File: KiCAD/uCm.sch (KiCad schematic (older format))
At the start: 29 parts, among them P1 AREF, P4 ICSP, P5 FTDI, SW1 Reset, SW2 INT0, SW3 INT1, U7 ATMEGA328-AU-ND, X1 16MHz

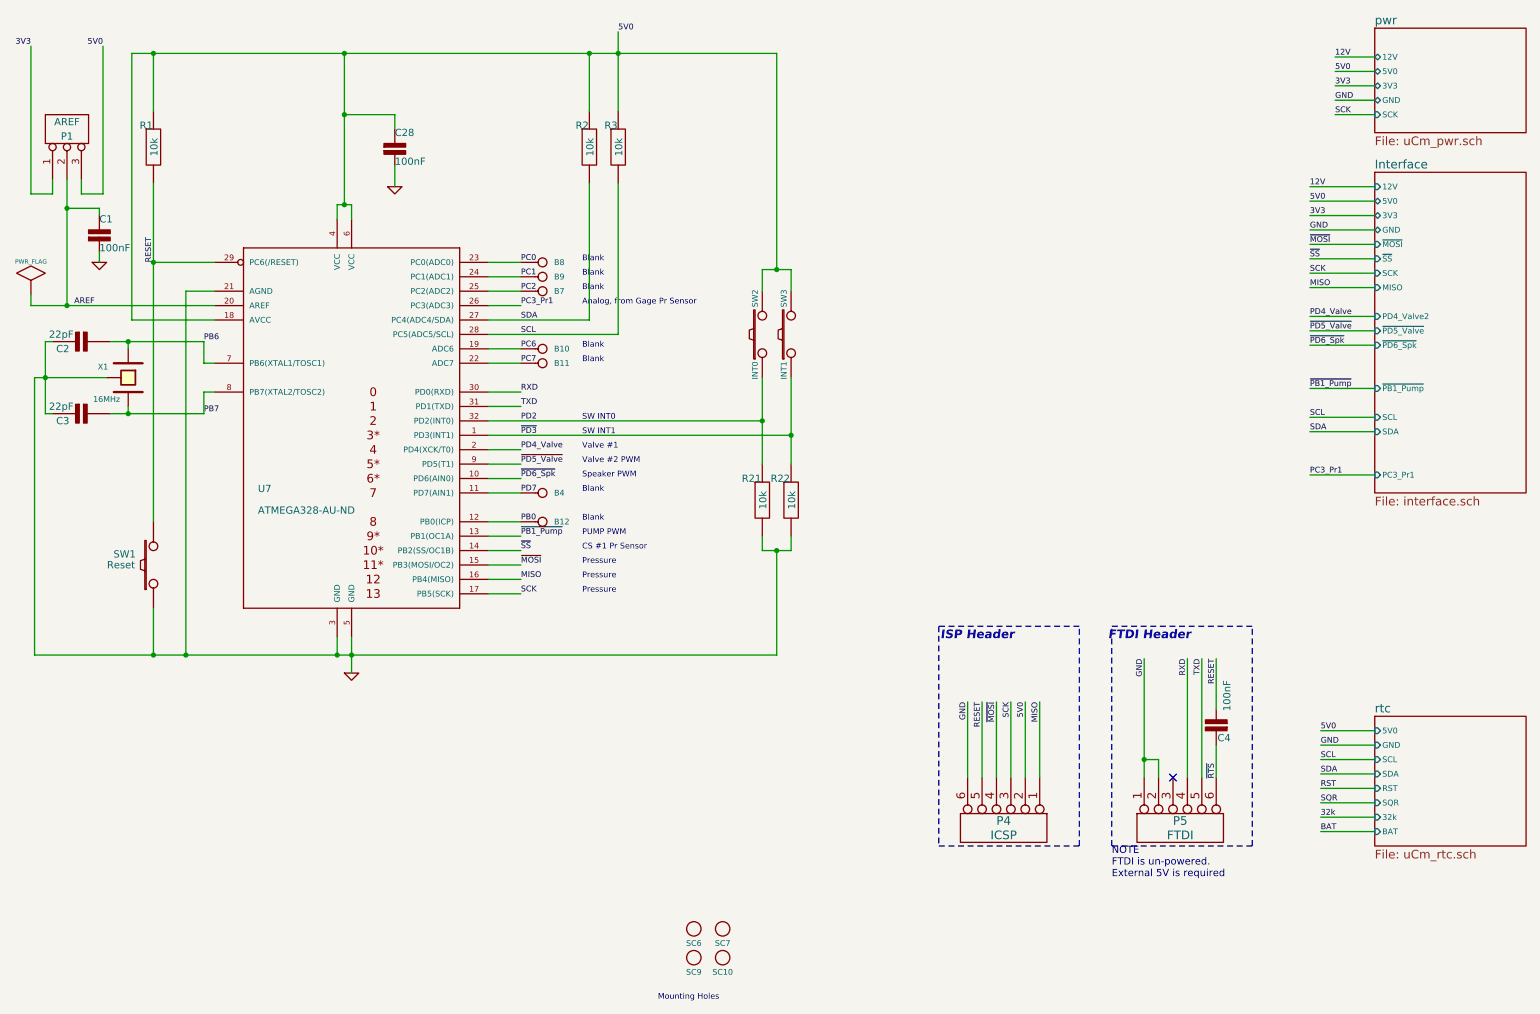
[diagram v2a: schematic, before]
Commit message: changed power supply section
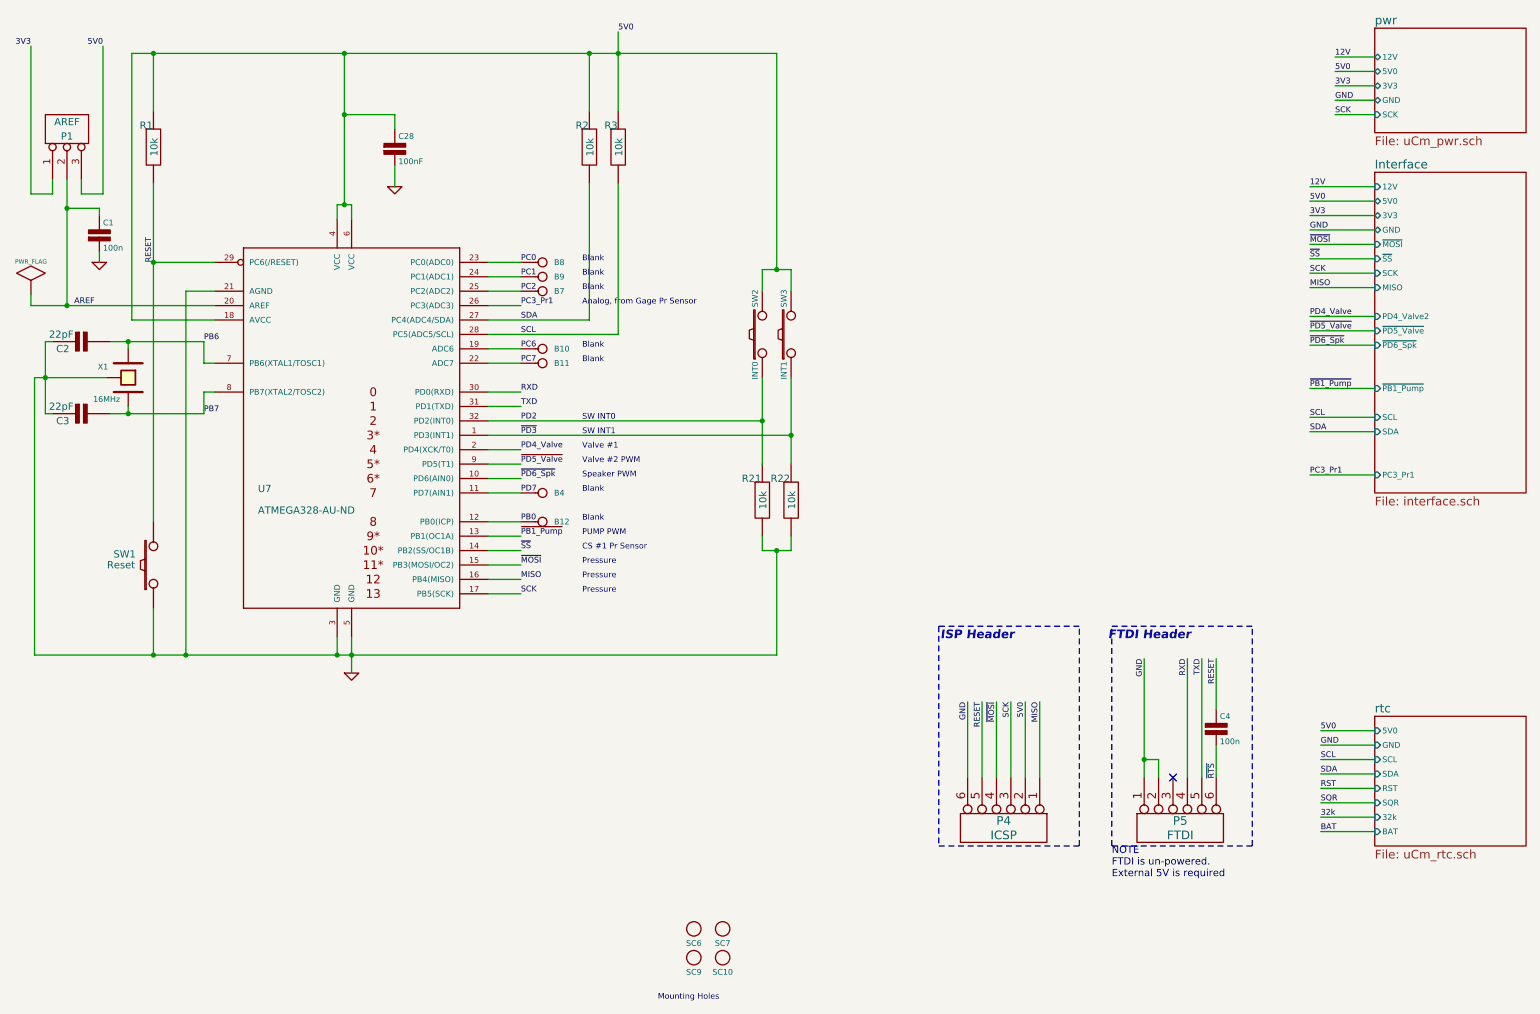
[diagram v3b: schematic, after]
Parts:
- C1, C4: value 100nF -> 100n; footprint uCm:c_0805 -> (none); Field10 399-5863-ND -> (none); Field11 http://www.digikey.com/product-detail/en/R82DC3100AA50J/399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 -> (none); Field4 CAP FILM 0.1UF 63VDC RADIAL -> (none); Field5 100nF, 63V -> (none); Field6 R82 -> (none); Field7 Kemet -> (none); Field8 R82DC3100AA50J -> (none); Field9 Digikey -> (none); manf# (none) -> CL21B104KCC5PNC
- C2, C3: Field10 BC1034CT-ND -> (none); Field11 http://www.digikey.com/product-detail/en/K220J15C0GF5TH5/BC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 -> (none); Field4 CAP CER 22PF 50V 5% RADIAL -> (none); Field5 22pF, 50V -> (none); Field6 Radial -> (none); Field7 Vishay BC Components -> (none); Field8 K220J15C0GF5TH5 -> (none); Field9 Digikey -> (none); manf# (none) -> CL10C220JB8NNNC
- C28: Field10 399-5863-ND -> (none); Field11 http://www.digikey.com/product-detail/en/R82DC3100AA50J/399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 -> (none); Field4 CAP FILM 0.1UF 63VDC RADIAL -> (none); Field5 100nF, 63V -> (none); Field6 R82 -> (none); Field7 Kemet -> (none); Field8 R82DC3100AA50J -> (none); Field9 Digikey -> (none); manf# (none) -> CL21B104KCC5PNC
- P1: Field10 SAM1031-50-ND -> (none); Field11 http://www.digikey.com/scripts/DkSearch/dksus.dll?WT.z_head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 -> (none); Field4 CONN HEADER 50POS .100\" SGL GOLD -> (none); Field5 Header, Unshrouded, Male pin, -> (none); Field6 0.1\" pitch x 50 nos -> (none); Field7 Samtec Inc -> (none); Field8 TSW-150-07-L-S -> (none); Field9 Digikey -> (none)
- P4: Field10 609-3210-ND -> (none); Field11 http://www.digikey.com/scripts/DkSearch/dksus.dll?vendor=0&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 -> (none); Field4 CONN HEADER 6POS .100 STR 15AU -> (none); Field5 Header, Unshrouded, Male Pin -> (none); Field6 6 pos, 2 row, 0.1\" -> (none); Field7 FCI -> (none); Field8 67996-206HLF -> (none); Field9 Digikey -> (none); manf# (none) -> PREC003DAAN-RC
- P5: manf# (none) -> PREC006SAAN-RC
- R1, R2, R21, R22, R3: Field10 CF18JT10K0CT-ND -> (none); Field11 http://www.digikey.com/product-detail/en/CF18JT10K0/CF18JT1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 -> (none); Field4 RES 10K OHM 1/8W 5% CF AXIAL -> (none); Field5 0.125W, 1/8W -> (none); Field6 Axial -> (none); Field7 Stackpole Electronics Inc -> (none); Field8 CF18JT10K0 -> (none); Field9 Digikey -> (none); manf# (none) -> RMCF0805JT10K0
- SW1, SW2, SW3: Field10 450-1649-ND -> (none); Field11 http://www.digikey.com/product-detail/en/FSM2JH/450-1649-ND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 -> (none); Field4 SWITCH TACTILE SPST-NO 0.05A 12V -> (none); Field5 SPST, NO -> (none); Field6 Top actuated 6.00mm x 6.00mm -> (none); Field7 TE Connectivity -> (none); Field8 FSM2JH -> (none); Field9 Digikey -> (none); manf# (none) -> FSMRA3JH
- U7: manf# (none) -> ATMEGA328-AU
- X1: Field10 X908-ND -> (none); Field11 http://www.digikey.com/product-detail/en/ZTT-16.00MX/X908-N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 -> (none); Field4 CER RESONATOR 16.00MHZ -> (none); Field5 16Mhz Ceramic built in capacitor -> (none); Field6 Radial - 3 Lead, 2.50mm Pitch -> (none); Field7 ECS Inc -> (none); Field8 ZTT-16.00MX -> (none); Field9 Digikey -> (none); manf# (none) -> TSX-3225 16.0000MF09Z-AC3
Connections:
- net RESET: now also C4.1; no longer C4.2
- net ~RTS: now also C4.2; no longer C4.1

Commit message: changed power supply section
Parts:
- C1, C4: footprint (none) -> uCm:c_0805
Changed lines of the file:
@@
 F 0 "C1" H 1225 2125 40  0000 L CNN
 F 1 "100n" H 1225 1950 40  0000 L CNN
-F 2 "" H 1200 2050 60  0000 C CNN
+F 2 "uCm:c_0805" H 1200 2050 60  0001 C CNN
 F 3 "" H 1200 2050 60  0000 C CNN
 F 4 "CL21B104KCC5PNC" H 1200 2250 60  0001 L CNN "manf#"
@@
 F 0 "C4" H 8975 5550 40  0000 L CNN
 F 1 "100n" H 8975 5375 40  0000 L CNN
-F 2 "" H 8950 5475 60  0000 C CNN
+F 2 "uCm:c_0805" H 8950 5475 60  0001 C CNN
 F 3 "" H 8950 5475 60  0000 C CNN
 F 4 "CL21B104KCC5PNC" H 8950 5675 60  0001 L CNN "manf#"
